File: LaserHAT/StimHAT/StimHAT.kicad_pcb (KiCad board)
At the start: 4 copper layers, 65 x 57 mm, 112 parts, among them J1 GPIO, J10 OLED 0.91 (GND VCC SCL SDA), J101 ELECTRODE E1/E2, J102 B4B-PH-K-S(LF)(SN), J103 5V TO DC-DC POD, J5 GT-USB-7010ASV, J6 BNC TRIGGER IN, J7 BNC STIM OUT, Q3 AP30P30Q, Q4 DMMT5401, Q5 AP30P30Q, SW10 MSK12C02, SW6 TS-1088-AR02016, SW7 SKRHADE010, SW9 TS-1088-AR02016, U1 M24C32-WDW6TP, U101 ISO7741FDBQR, U104 TLV76050DBZR, U105 DAC60501ZDGSR, U106 OPA2192IDGKR, U107 CD74HC4053PWR, U108 DG418DY-T1-E3, U109 ISO1640BDR, U110 TLV1702AIDGKR, U4 MCP1700T-3302E/MB, U5 AP2171W, U6 CH340N, U7 MSPM0G1507SRHBR, U8 74LVC2G17GW

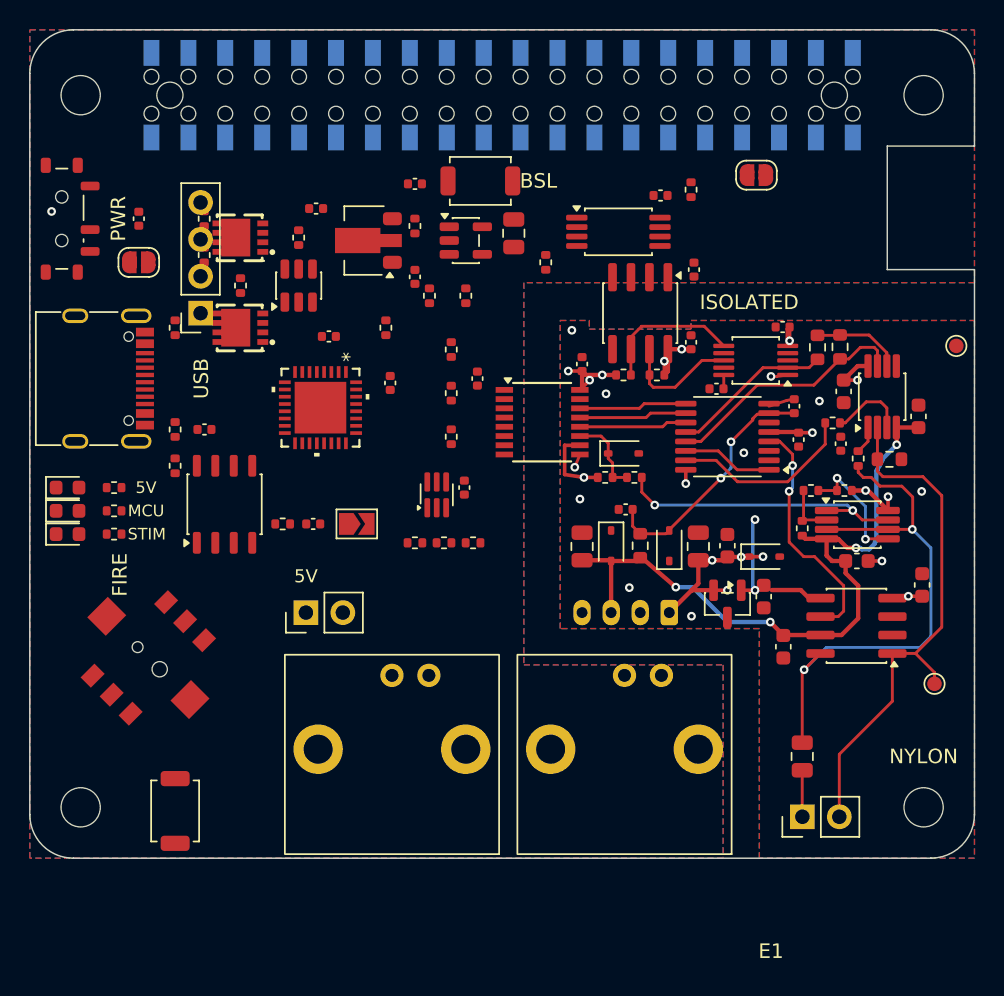
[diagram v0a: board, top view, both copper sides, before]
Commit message: StimHAT: J10 kept where the user put it (Q5, R21, Q3, R8, R19, R20 moved out of its column), OLED drawn flat eastward; isolated power re-laid as a clean grid on In2 (+5V_ISO, +V_STIM) and the back (-V_STIM, -5V_ISO); DRC 0 errors
Co-Authored-By: Claude Fable 5.1 <noreply@anthropic.com>
Claude-Session: https://claude.ai/code/session_015kiXLxnPpBaXdXJu2EMvn7
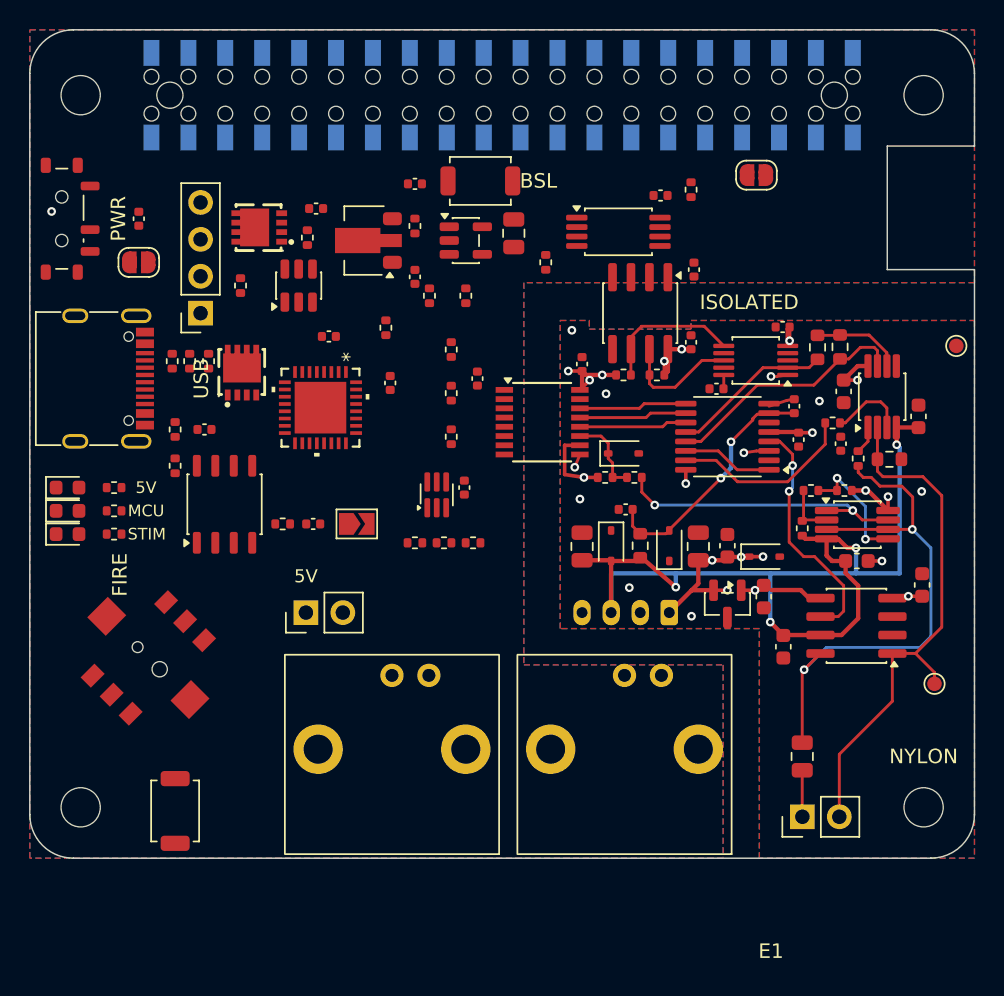
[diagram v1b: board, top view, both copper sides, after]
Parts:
- moved R20 9.80 mm to (12.3, 22.8)
- moved R19 7.37 mm to (11.0, 22.8)
- moved Q3 3.10 mm to (14.6, 23.6), turned to 0 degrees
- moved R8 2.31 mm to (9.80, 22.8)
- moved Q5 1.48 mm to (15.8, 13.6)
- moved R21 0.60 mm to (19.1, 14.3)
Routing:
- net -V_STIM: track 48.0 -> 69.1 mm
- net +5V_ISO: track 76.2 -> 87.7 mm, vias 12 -> 11
- net +V_STIM: track 58.5 -> 65.6 mm
- net GND_ISO: track 2.74 -> 4.48 mm
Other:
- board text added: "0.91in OLED module on J10: pins on its west (short) edge, right-angle pins into the vertical socket, lying flat eastward 8.5 mm up"
- board text removed: "0.91in OLED module on J10 (vertical socket): straight pins -> standing along the header (strip), right-angle pins -> lying flat (rect)"
